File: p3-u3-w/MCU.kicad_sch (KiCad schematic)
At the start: 20 parts, among them U1 STM32WB55CEUx, X1 NX2016SA-32MHZ-EXS00A-CS06654, Y1 32k768

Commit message: added in some buttons and pinout.
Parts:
- removed U1: STM32WB55CEUx, Package_DFN_QFN:QFN-48-1EP_7x7mm_P0.5mm_EP5.6x5.6mm, symbol MCU_ST_STM32WB:STM32WB55CEUx
- added C16: 100nF, symbol Device:C
- added J1: SWD_pin, symbol Connector:Conn_01x04_Pin
- added R1: 100k, symbol Device:R
- added R2: 10k, symbol Device:R
- added SW1: SW_SPST, symbol Switch:SW_SPST
- added U2: STM32WB55RGVx, Package_DFN_QFN:QFN-68-1EP_8x8mm_P0.4mm_EP6.4x6.4mm, symbol MCU_ST_STM32WB:STM32WB55RGVx
- C7: value 10nF -> 100nF
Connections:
- net +3V3: now also J1.2 (Pin_2), R1.1, SW1.2 (B), U2.1 (VBAT), U2.13 (VREF+), U2.14 (VDDA), U2.30 (VDD), U2.33 (VDDRF), U2.44 (VDDSMPS), U2.45 (VDD), U2.68 (VDD)
- net GND: now also C16.1, J1.1 (Pin_1), R2.1, U2.32 (VSSRF), U2.42 (VSSSMPS), U2.69 (VSS)
- net OSC_IN: now also U2.35 (OSC_IN)
- net OSC_OUT: now also U2.34 (OSC_OUT)
- net VDDUSB: now also U2.55 (VDDUSB)
- net at C15.2, Y1.1: now also U2.3 (PC14)
- net at C14.2, Y1.2: now also U2.4 (PC15)
- net at L1.2: now also U2.43 (VLXSMPS)
- net at C13.2, L2.2: now also U2.41 (VFBSMPS)
- new net: C16.2, R1.2, U2.8 (NRST)
- new net: R2.2, SW1.1 (A), U2.5 (PH3)
- new net I2C_SCL: U2.6 (PB8)
- new net I2C_SDA: U2.51 (PA10)
- new net I2S_FS: U2.7 (PB9)
- new net I2S_SCK: U2.23 (PA8)
- new net I2S_SD: U2.12 (PC3)
- new net SWCLK: J1.4 (Pin_4), U2.56 (PA14)
- new net SWDIO: J1.3 (Pin_3), U2.54 (PA13)
- new net USB_DM: U2.52 (PA11)
- new net USB_DP: U2.53 (PA12)
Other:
- moved on the sheet: C13, C14, C15, L1, L2, Y1

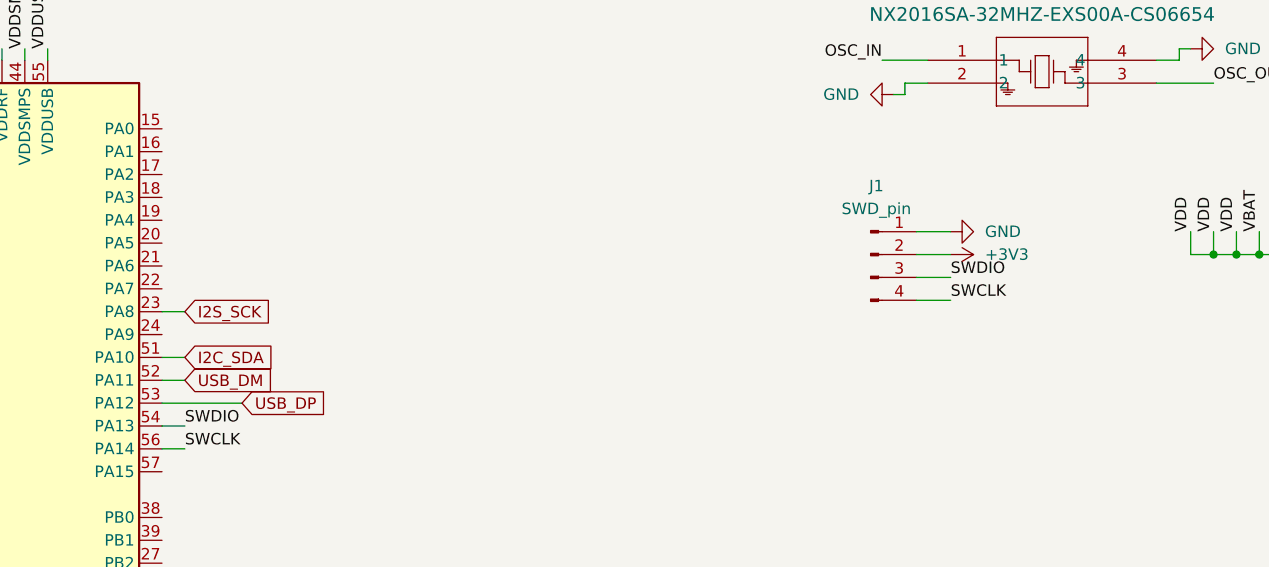
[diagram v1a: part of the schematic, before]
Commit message: added in i2C pullups, added in display
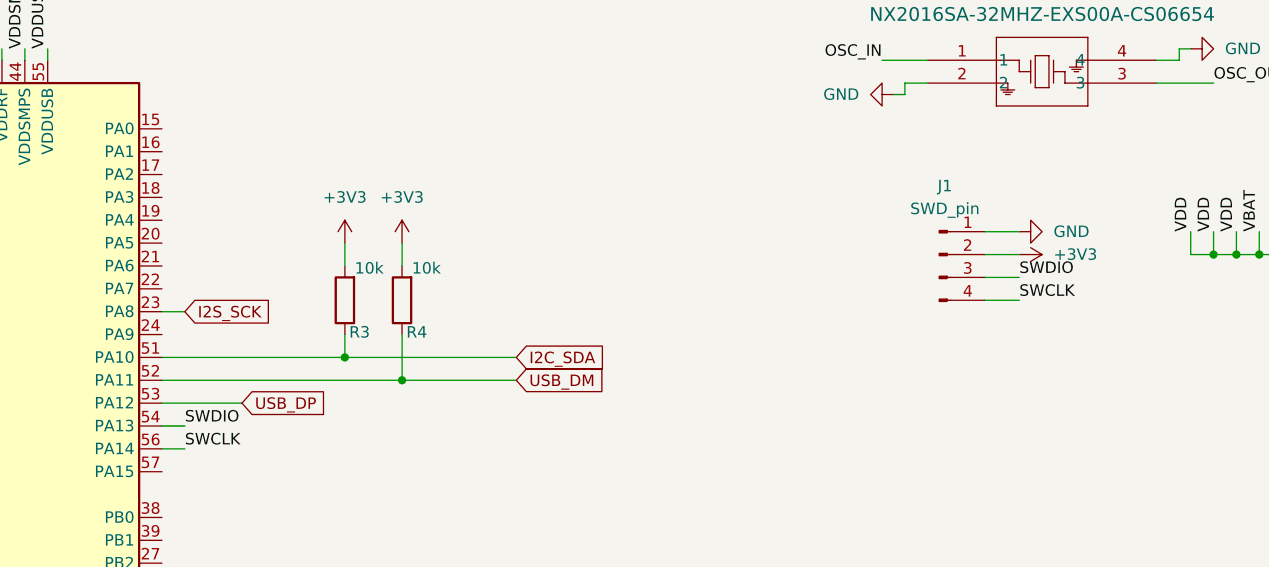
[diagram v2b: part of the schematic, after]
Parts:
- added R3, R4: 10k, symbol Device:R
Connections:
- net +3V3: now also R3.2, R4.2
- net I2C_SDA: now also R3.1
- net USB_DM: now also R4.1
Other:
- moved on the sheet: J1

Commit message: added in power side and mostly finished schematics :)
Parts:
- removed C13: 4.7uF, symbol Device:C
- removed C14, C15: 10pF, symbol Device:C
- removed C16: 100nF, symbol Device:C
- removed L1: 10nH, symbol Device:L
- removed L2: 10uH, symbol Device:L
- removed R1: 100k, symbol Device:R
- removed R2: 10k, symbol Device:R
- removed SW1: SW_SPST, symbol Switch:SW_SPST
- removed U2: STM32WB55RGVx, Package_DFN_QFN:QFN-68-1EP_8x8mm_P0.4mm_EP6.4x6.4mm, symbol MCU_ST_STM32WB:STM32WB55RGVx
- removed Y1: 32k768, symbol Device:Crystal
- added C30, C31: 10pF, symbol Device:C
- added C32: 100nF, symbol Device:C
- added C33: 4.7uF, symbol Device:C
- added L3: 10uH, symbol Device:L
- added L4: 10nH, symbol Device:L
- added R15: 10k, symbol Device:R
- added R16: 100k, symbol Device:R
- added SW2: SW_SPST, symbol Switch:SW_SPST
- added U3: STM32WB55CEUx, Package_DFN_QFN:QFN-48-1EP_7x7mm_P0.5mm_EP5.6x5.6mm, symbol MCU_ST_STM32WB:STM32WB55CEUx
- added Y2: 32k768, symbol Device:Crystal
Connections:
- net +3V3: now also R16.1, SW2.2 (B), U3.1 (VBAT), U3.20 (VDD), U3.23 (VDDRF), U3.34 (VDDSMPS), U3.35 (VDD), U3.48 (VDD), U3.8 (VDDA)
- net GND: now also C30.1, C31.1, C32.1, C33.1, R15.1, U3.22 (VSSRF), U3.32 (VSSSMPS), U3.49 (VSS)
- net I2C_SCL: now also R4.1, U3.5 (PB8)
- net I2C_SDA: now also U3.6 (PB9)
- net I2S_FS: now also U3.18 (PA9)
- net I2S_SCK: now also U3.17 (PA8)
- net I2S_SD: now also U3.36 (PA10)
- net OSC_IN: now also U3.25 (OSC_IN)
- net OSC_OUT: now also U3.24 (OSC_OUT)
- net SWCLK: now also U3.41 (PA14)
- net SWDIO: now also U3.39 (PA13)
- net USB_DM: now also U3.37 (PA11); no longer R4.1
- net USB_DP: now also U3.38 (PA12)
- net VDDUSB: now also U3.40 (VDDUSB)
- new net: R15.2, SW2.1 (A), U3.4 (PH3)
- new net: C33.2, L3.2, U3.31 (VFBSMPS)
- new net: C31.2, U3.3 (PC15), Y2.2
- new net: C32.2, R16.2, U3.7 (NRST)
- new net: C30.2, U3.2 (PC14), Y2.1
- new net: L4.2, U3.33 (VLXSMPS)
- new net: L3.1, L4.1
- new net BAT_SENSE: U3.9 (PA0)
- new net BTN_MENU: U3.45 (PB5)
- new net BTN_NEXT: U3.44 (PB4)
- new net BTN_PLY: U3.19 (PB2)
- new net BTN_PREV: U3.43 (PB3)
- new net BTN_VOL+: U3.29 (PB1)
- new net BTN_VOL-: U3.28 (PB0)
- new net IMU_INT1: U3.46 (PB6)
- new net IMU_INT2: U3.42 (PA15)
- new net IMU_SAO: U3.47 (PB7)
- new net SPI_CS: U3.13 (PA4)
- new net SPI_MISO: U3.15 (PA6)
- new net SPI_MOSI: U3.16 (PA7)
- new net SPI_SCK: U3.14 (PA5)
- new net UART_RX: U3.12 (PA3)
- new net UART_TX: U3.11 (PA2)
- no-connect marks 1 -> 2
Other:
- note added: "Do RF stuff here.."
- moved on the sheet: J1, R3, R4, X1

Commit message: finished schematics, started routing and layout.
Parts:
- added C41: 0.8pF, Capacitor_SMD:C_0603_1608Metric, symbol Device:C
- added C42: 0.3pF, Capacitor_SMD:C_0603_1608Metric, symbol Device:C
- added J8: CONMHF1-SMD-G-T, CONMHF1-SMD-G-T:COAX3_CONMHF1-SMD-G-T_TEC, symbol 2026-08-19_14-33-22:CONMHF1-SMD-G-T
- added L2: 2.7nH, Inductor_SMD:L_0603_1608Metric, symbol Device:L
- added U7: DLF162500LT-5028A1, DLF162500LT:DLF-4_1P6X0P8, symbol 2026-08-19_14-10-11:DLF162500LT-5028A1
- C1, C10, C11, C12, C2, C3, C30, C31, C32, C33, C4, C5, C6, C7, C8, C9: footprint (none) -> Capacitor_SMD:C_0603_1608Metric
- J1: footprint (none) -> Connector_PinHeader_1.00mm:PinHeader_1x04_P1.00mm_Vertical
- L3, L4: footprint (none) -> Inductor_SMD:L_0603_1608Metric
- R15, R16, R3, R4: footprint (none) -> Resistor_SMD:R_0603_1608Metric
- SW2: footprint (none) -> Button_Switch_SMD:Panasonic_EVQPUL_EVQPUC
- X1: footprint NX2016SA_NDK -> NX2016SA-32MHZ-EXS00A-CS06654:NX2016SA_NDK
- Y2: footprint (none) -> Crystal:Crystal_SMD_3215-2Pin_3.2x1.5mm
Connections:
- net VDDUSB is gone; now on net +3V3: C12.2, U3.40 (VDDUSB)
- net GND: now also C41.2, C42.2, J8.2 (GND), J8.3 (GND), J8.4 (GND), U7.2 (GND), U7.4 (GND)
- net RF1: now reaches U3.21 (RF1)
- net RF1: now also C41.1, L2.1
- new net: C42.1, L2.2, U7.1 (IN)
- new net: J8.1 (SIGNAL), U7.3 (OUT)
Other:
- note removed: "Do RF stuff here.."

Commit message: changed some routing
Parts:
- C1, C10, C11, C12, C2, C3, C30, C31, C32, C33, C4, C41, C42, C5, C6, C7, C8, C9: footprint Capacitor_SMD:C_0603_1608Metric -> Capacitor_SMD:C_0402_1005Metric
- R15, R16, R3, R4: footprint Resistor_SMD:R_0603_1608Metric -> Resistor_SMD:R_0402_1005Metric
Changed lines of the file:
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@@
 			)
 		)
-		(property "Footprint" "Capacitor_SMD:C_0603_1608Metric"
+		(property "Footprint" "Capacitor_SMD:C_0402_1005Metric"
 			(at 54.3052 156.21 0)
 			(effects
@@
 			)
 		)
-		(property "Footprint" "Capacitor_SMD:C_0603_1608Metric"
+		(property "Footprint" "Capacitor_SMD:C_0402_1005Metric"
 			(at 38.1 58.1152 0)
 			(effects
@@
 			)
 		)
-		(property "Footprint" "Capacitor_SMD:C_0603_1608Metric"
+		(property "Footprint" "Capacitor_SMD:C_0402_1005Metric"
 			(at 234.6452 55.88 0)
 			(effects
@@
 			)
 		)
-		(property "Footprint" "Capacitor_SMD:C_0603_1608Metric"
+		(property "Footprint" "Capacitor_SMD:C_0402_1005Metric"
 			(at 48.5648 87.63 0)
 			(effects
@@
 			)
 		)
-		(property "Footprint" "Capacitor_SMD:C_0603_1608Metric"
+		(property "Footprint" "Capacitor_SMD:C_0402_1005Metric"
 			(at 262.5852 55.88 0)
 			(effects
@@
 			)
 		)
-		(property "Footprint" "Capacitor_SMD:C_0603_1608Metric"
+		(property "Footprint" "Capacitor_SMD:C_0402_1005Metric"
 			(at 46.99 39.0652 0)
 			(effects
@@
 			)
 		)
-		(property "Footprint" "Capacitor_SMD:C_0603_1608Metric"
+		(property "Footprint" "Capacitor_SMD:C_0402_1005Metric"
 			(at 244.8052 55.88 0)
 			(effects
@@
 			)
 		)
-		(property "Footprint" "Capacitor_SMD:C_0603_1608Metric"
+		(property "Footprint" "Capacitor_SMD:C_0402_1005Metric"
 			(at 262.5852 110.49 0)
 			(effects
@@
 			)
 		)
-		(property "Footprint" "Capacitor_SMD:C_0603_1608Metric"
+		(property "Footprint" "Capacitor_SMD:C_0402_1005Metric"
 			(at 72.0852 156.21 0)
 			(effects
@@
 			)
 		)
-		(property "Footprint" "Capacitor_SMD:C_0603_1608Metric"
+		(property "Footprint" "Capacitor_SMD:C_0402_1005Metric"
 			(at 271.4752 110.49 0)
 			(effects
@@
 			)
 		)
-		(property "Footprint" "Resistor_SMD:R_0603_1608Metric"
+		(property "Footprint" "Resistor_SMD:R_0402_1005Metric"
 			(at 135.128 93.98 90)
 			(effects
@@
 			)
 		)
-		(property "Footprint" "Capacitor_SMD:C_0603_1608Metric"
+		(property "Footprint" "Capacitor_SMD:C_0402_1005Metric"
 			(at 270.2052 142.24 0)
 			(effects
@@
 			)
 		)
-		(property "Footprint" "Resistor_SMD:R_0603_1608Metric"
+		(property "Footprint" "Resistor_SMD:R_0402_1005Metric"
 			(at 47.752 31.75 90)
 			(effects
@@
 			)
 		)
-		(property "Footprint" "Capacitor_SMD:C_0603_1608Metric"
+		(property "Footprint" "Capacitor_SMD:C_0402_1005Metric"
 			(at 261.3152 83.82 0)
 			(effects
@@
 			)
 		)
-		(property "Footprint" "Capacitor_SMD:C_0603_1608Metric"
+		(property "Footprint" "Capacitor_SMD:C_0402_1005Metric"
 			(at 37.7952 87.63 0)
 			(effects
@@
 			)
 		)
-		(property "Footprint" "Capacitor_SMD:C_0603_1608Metric"
+		(property "Footprint" "Capacitor_SMD:C_0402_1005Metric"
 			(at 261.3152 26.67 0)
 			(effects
@@
 			)
 		)
-		(property "Footprint" "Capacitor_SMD:C_0603_1608Metric"
+		(property "Footprint" "Capacitor_SMD:C_0402_1005Metric"
 			(at 253.6952 55.88 0)
 			(effects
@@
 			)
 		)
-		(property "Footprint" "Capacitor_SMD:C_0603_1608Metric"
+		(property "Footprint" "Capacitor_SMD:C_0402_1005Metric"
 			(at 271.4752 26.67 0)
 			(effects
@@
 			)
 		)
-		(property "Footprint" "Capacitor_SMD:C_0603_1608Metric"
+		(property "Footprint" "Capacitor_SMD:C_0402_1005Metric"
 			(at 271.4752 55.88 0)
 			(effects
@@
 			)
 		)
-		(property "Footprint" "Resistor_SMD:R_0603_1608Metric"
+		(property "Footprint" "Resistor_SMD:R_0402_1005Metric"
 			(at 43.18 70.612 90)
 			(effects
@@
 			)
 		)
-		(property "Footprint" "Capacitor_SMD:C_0603_1608Metric"
+		(property "Footprint" "Capacitor_SMD:C_0402_1005Metric"
 			(at 271.4752 83.82 0)
 			(effects
@@
 			)
 		)
-		(property "Footprint" "Resistor_SMD:R_0603_1608Metric"
+		(property "Footprint" "Resistor_SMD:R_0402_1005Metric"
 			(at 128.778 93.98 90)
 			(effects

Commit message: added in some more routing.
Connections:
- net +3V3 renamed +3.3V
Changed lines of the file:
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@@
 	(wire
 		(pts
+			(xy 125.73 24.13) (xy 128.27 24.13)
+		)
+		(stroke
+			(width 0)
+			(type default)
+		)
+	)
+	(wire
+		(pts
 			(xy 127 87.63) (xy 127 90.17)
 		)
@@
 	)
 	(symbol
+		(lib_id "power:+3V3")
+		(at 125.73 24.13 90)
+		(unit 1)
+		(exclude_from_sim no)
+		(in_bom yes)
+		(on_board yes)
+		(dnp no)
+		(fields_autoplaced yes)
+		(property "Reference" "#PWR0125"
+			(at 129.54 24.13 0)
+			(effects
+				(font
+					(size 1.27 1.27)
+				)
+				(hide yes)
+			)
+		)
+		(property "Value" "+3V3"
+			(at 121.92 24.1299 90)
+			(effects
+				(font
+					(size 1.27 1.27)
+				)
+				(justify left)
+			)
+		)
+		(property "Footprint" ""
+			(at 125.73 24.13 0)
+			(effects
+				(font
+					(size 1.27 1.27)
+				)
+				(hide yes)
+			)
+		)
+		(property "Datasheet" ""
+			(at 125.73 24.13 0)
+			(effects
+				(font
+					(size 1.27 1.27)
+				)
+				(hide yes)
+			)
+		)
+		(property "Description" "Power symbol creates a global label with name \"+3V3\""
+			(at 125.73 24.13 0)
+			(effects
+				(font
+					(size 1.27 1.27)
+				)
+				(hide yes)
+			)
+		)
+		(pin "1"
+		)
+		(instances
+			(project "p3-u3-w"
+				(path "/afed05dd-3bce-4903-b4b6-a2a13f579b42/0c00c70c-6ec5-4958-b79d-f19affab4d31"
+					(reference "#PWR0125")
+					(unit 1)
+				)
+			)
+		)
+	)
+	(symbol
 		(lib_id "Device:C")
 		(at 243.84 59.69 0)
@@
 					(unit 1)
 				)
+			)
+		)
+	)
+	(symbol
+		(lib_id "power:+3.3V")
+		(at 128.27 24.13 270)
+		(unit 1)
+		(exclude_from_sim no)
+		(in_bom yes)
+		(on_board yes)
+		(dnp no)
+		(fields_autoplaced yes)
+		(property "Reference" "#PWR0126"
+			(at 124.46 24.13 0)
+			(effects
+				(font
+					(size 1.27 1.27)
+				)
+				(hide yes)
+			)
+		)
+		(property "Value" "+3.3V"
+			(at 132.08 24.1299 90)
+			(effects
+				(font
+					(size 1.27 1.27)
+				)
+				(justify left)
+			)
+		)
+		(property "Footprint" ""
+			(at 128.27 24.13 0)
+			(effects
+				(font
+					(size 1.27 1.27)
+				)
+				(hide yes)
+			)
+		)
+		(property "Datasheet" ""
+			(at 128.27 24.13 0)
+			(effects
+				(font
+					(size 1.27 1.27)
+				)
+				(hide yes)
+			)
+		)
+		(property "Description" "Power symbol creates a global label with name \"+3.3V\""
+			(at 128.27 24.13 0)
+			(effects
+				(font
+					(size 1.27 1.27)
+				)
+				(hide yes)
+			)
+		)
+		(pin "1"
+		)
+		(instances
+			(project ""
+				(path "/afed05dd-3bce-4903-b4b6-a2a13f579b42/0c00c70c-6ec5-4958-b79d-f19affab4d31"
+					(reference "#PWR0126")
+					(unit 1)
+				)

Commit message: did some more routing.
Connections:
- net BTN_NEXT: now also U3.29 (PB1); no longer U3.44 (PB4)
- net BTN_PREV: now also U3.28 (PB0); no longer U3.43 (PB3)
- net BTN_VOL+: now also U3.44 (PB4); no longer U3.29 (PB1)
- net BTN_VOL-: now also U3.43 (PB3); no longer U3.28 (PB0)

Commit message: finished the pcb, added in BOM
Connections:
- net UART_RX: no longer names the net of U3.12 (PA3)
- net UART_TX: no longer names the net of U3.11 (PA2)
- no-connect marks 2 -> 4
